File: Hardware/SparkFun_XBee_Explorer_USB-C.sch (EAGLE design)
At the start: 54 parts, among them J3 USB Female Type C Connector, J4 QWIIC_RIGHT_ANGLE, U2 AP63203, U5 ESD Diode, U7 FT231XS

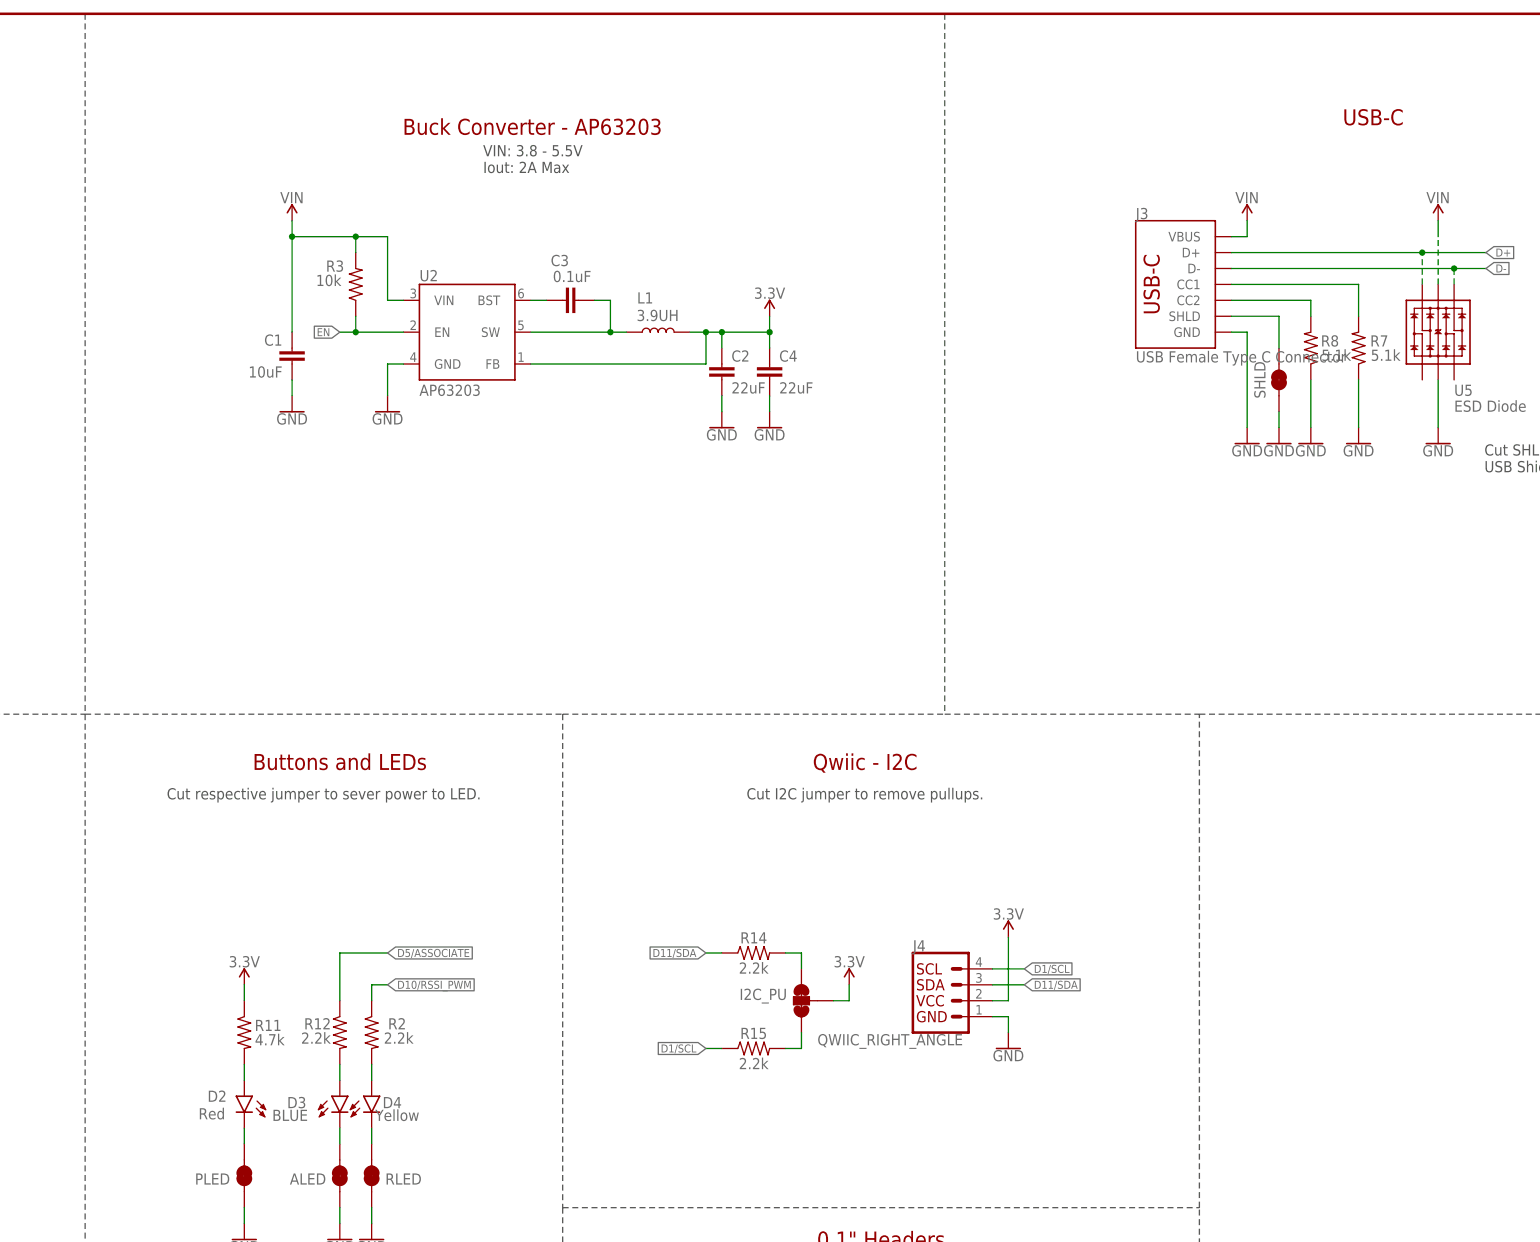
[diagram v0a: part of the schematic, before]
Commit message: Adds 4.7uF decoupling cap to FTDI
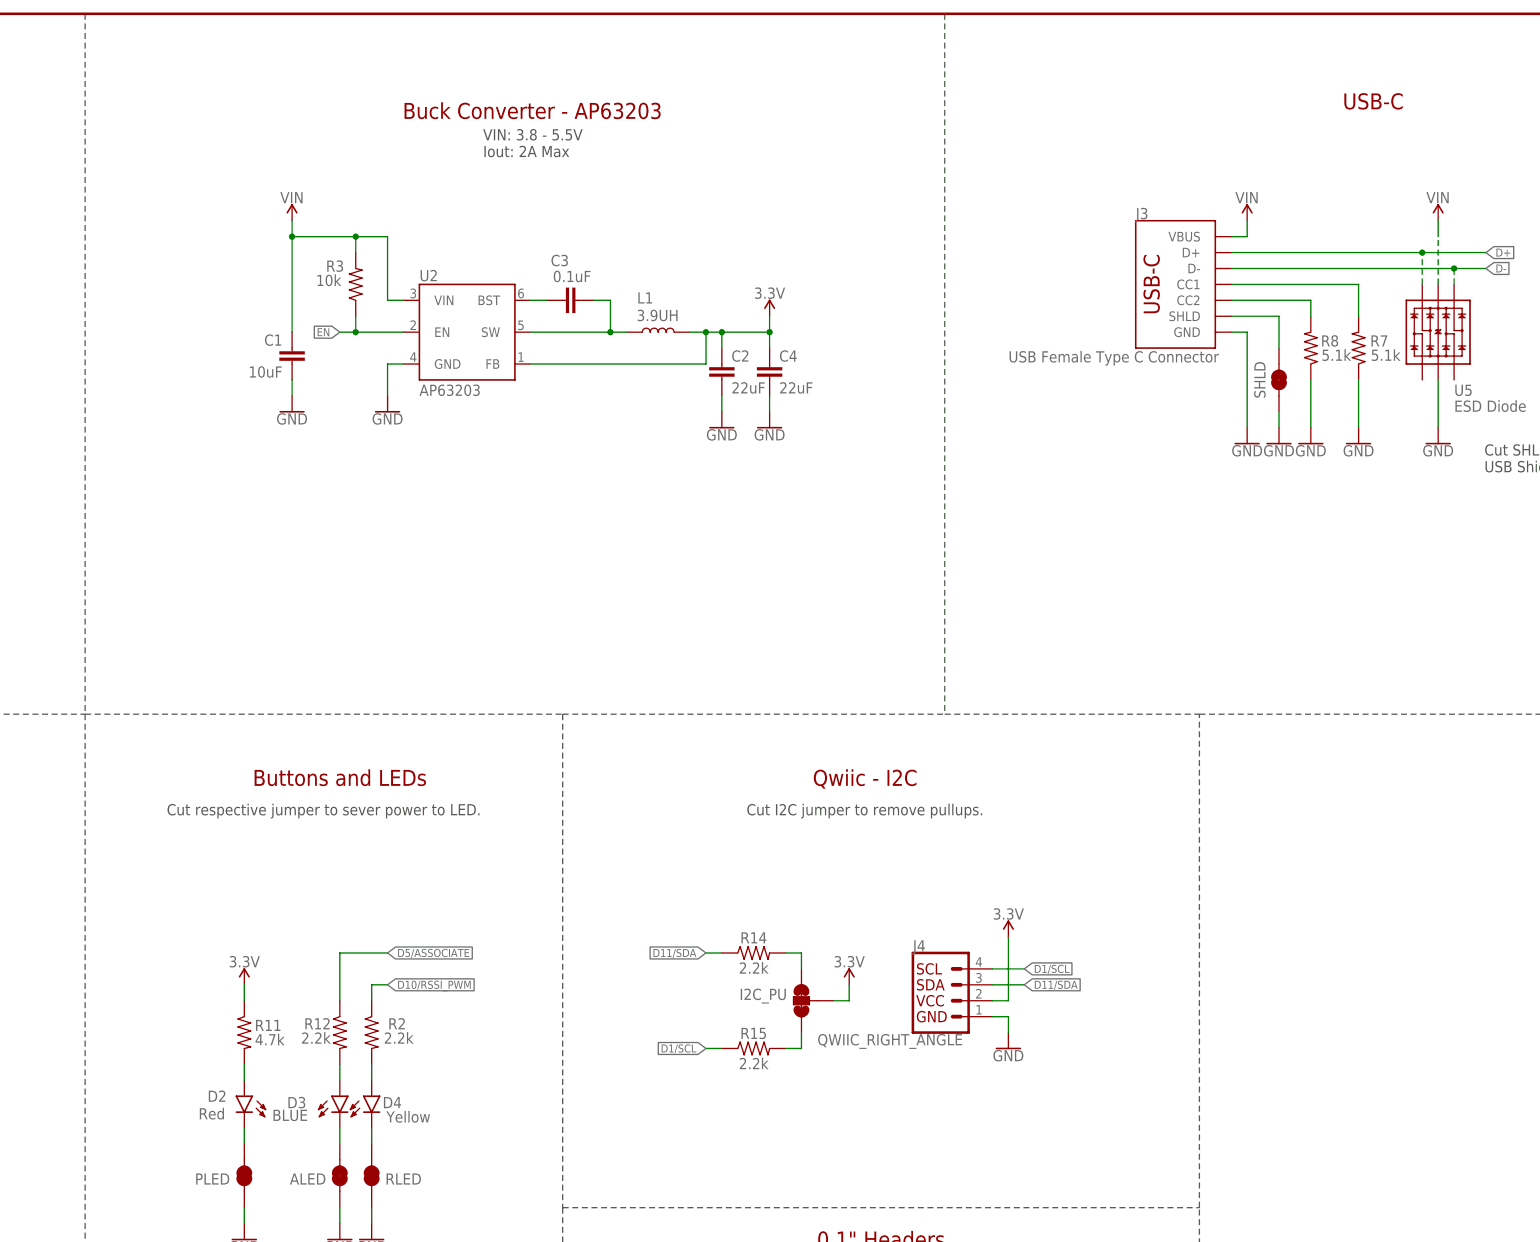
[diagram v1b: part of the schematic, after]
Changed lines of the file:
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@@
 <plain>
 <text x="60.96" y="259.08" size="1.778" layer="97" font="vector">VCC Range: 3.3V - 4.3V</text>
-<text x="223.774" y="261.366" size="2.54" layer="94" font="vector" align="center">Buck Converter - AP63203</text>
-<text x="276.86" y="160.02" size="2.54" layer="94" font="vector" align="center">Qwiic - I2C</text>
+<text x="223.774" y="263.906" size="2.54" layer="94" font="vector" align="center">Buck Converter - AP63203</text>
+<text x="276.86" y="157.48" size="2.54" layer="94" font="vector" align="center">Qwiic - I2C</text>
 <text x="424.18" y="7.62" size="2.54" layer="94" font="vector" align="center">v10</text>
 <text x="363.22" y="10.16" size="2.54" layer="94" font="vector" align="center">Elias Santistevan</text>
-<text x="193.04" y="160.02" size="2.54" layer="94" font="vector" align="center">Buttons and LEDs</text>
-<text x="215.9" y="254" size="1.778" layer="97" font="vector">VIN: 3.8 - 5.5V
+<text x="193.04" y="157.48" size="2.54" layer="94" font="vector" align="center">Buttons and LEDs</text>
+<text x="215.9" y="256.54" size="1.778" layer="97" font="vector">VIN: 3.8 - 5.5V
 Iout: 2A Max</text>
-<text x="276.86" y="154.94" size="1.778" layer="97" font="vector" align="center">Cut I2C jumper to remove pullups.</text>
-<text x="190.5" y="154.94" size="1.778" layer="97" font="vector" align="center">Cut respective jumper to sever power to LED.</text>
+<text x="276.86" y="152.4" size="1.778" layer="97" font="vector" align="center">Cut I2C jumper to remove pullups.</text>
+<text x="190.5" y="152.4" size="1.778" layer="97" font="vector" align="center">Cut respective jumper to sever power to LED.</text>
 <text x="76.2" y="264.16" size="2.54" layer="94" font="vector" align="center">RF Module - XBee 3 </text>
 <text x="279.4" y="83.82" size="2.54" layer="94" font="vector" align="center">0.1" Headers</text>
@@
 <wire x1="228.6" y1="88.9" x2="330.2" y2="88.9" width="0.1524" layer="97" style="shortdash"/>
 <text x="78.74" y="157.48" size="2.54" layer="94" font="vector" align="center">USB to UART - FT231XS</text>
-<text x="353.06" y="261.62" size="2.54" layer="94" font="vector">USB-C </text>
+<text x="353.06" y="264.16" size="2.54" layer="94" font="vector">USB-C </text>
 </plain>
 <instances>
@@
 <instance part="D4" gate="G$1" x="198.12" y="106.68" smashed="yes">
 <attribute name="NAME" x="202.946" y="106.553" size="1.778" layer="95" font="vector" rot="R180"/>
-<attribute name="VALUE" x="205.74" y="102.743" size="1.778" layer="96" font="vector" rot="R180" align="top-left"/>
+<attribute name="VALUE" x="207.518" y="102.489" size="1.778" layer="96" font="vector" rot="R180" align="top-left"/>
 </instance>
 <instance part="R2" gate="G$1" x="198.12" y="116.84" smashed="yes" rot="MR270">
@@
 </instance>
 <instance part="J3" gate="J1" x="322.58" y="236.22" smashed="yes">
-<attribute name="VALUE" x="320.04" y="223.774" size="1.778" layer="96" font="vector" rot="MR180" align="top-left"/>
+<attribute name="VALUE" x="299.72" y="223.774" size="1.778" layer="96" font="vector" rot="MR180" align="top-left"/>
 <attribute name="NAME" x="320.04" y="246.634" size="1.778" layer="95" font="vector"/>
 </instance>
